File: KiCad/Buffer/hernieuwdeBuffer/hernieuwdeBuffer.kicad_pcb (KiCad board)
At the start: 2 copper layers, 90.2 x 77.5 mm, 38 parts, among them J1 Conn_01x04_Female, J2 12V DC, J3 Rood, J4 Groen, J5 Oranje1, J6 Oranje2, SW1 ENABLE, SW2 BOOT, T1 signaal oranje, T10 o3r, T11 o4r, T12 o5r, T13 06r, T14 r1, T15 r2, T16 r3, T17 r4, T18 r5, T19 g1, T2 o1g, T20 g2, T21 g3, T22 g4, T23 g5, T3 o2g, T4 o3g, T5 o4g, T6 o5g, T7 06g, T8 o1r, T9 o2r, U1 ESP32-WROOM-32E_(16MB)

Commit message: kicad
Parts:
- R1: footprint libraries:RESC6332X65N -> Resistor_SMD:R_0805_2012Metric
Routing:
- net Net-(C1-Pad2): track 20.9 -> 21.9 mm, vias 0 -> 1

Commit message: updates standaard schema
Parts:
- added C1: 1u, Capacitor_SMD:C_0805_2012Metric, F.Cu at (138.0, 145.7)
- added R1: 10k, libraries:RESC6332X65N, F.Cu at (120.3, 154.2)
- added R2: 10k, libraries:RESC6332X65N, F.Cu at (129.0, 154.2)
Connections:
- SW1 pad 1: Net-(C1-Pad2) -> Net-(U1-Pad25)
- SW1 pad 2: Net-(C1-Pad2) -> Net-(U1-Pad3)
- SW2 pad 1: Net-(SW2-Pad1) -> Net-(U1-Pad25)
- SW2 pad 2: Net-(SW2-Pad1) -> Net-(U1-Pad25)
- U1 pad 25: Net-(SW2-Pad1) -> Net-(U1-Pad25)
- U1 pad 3: Net-(R1-Pad2) -> Net-(U1-Pad3)
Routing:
- net r5: track 15.6 -> 0.00 mm, vias 1 -> 0
- net GND: track 209.5 -> 225.1 mm, vias 0 -> 1
- net Net-(U1-Pad25): track 0.00 -> 11.3 mm
- net Net-(SW2-Pad1): track 11.3 -> 0.00 mm
- net Net-(C1-Pad2): track 21.9 -> 13.4 mm
- net Net-(U1-Pad3): track 0.00 -> 3.77 mm
- net Net-(R1-Pad2): track 3.77 -> 0.00 mm

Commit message: kicad aanpassingen buffer
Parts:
- removed the C1 at (105.0, 75.8)
- removed the R1 at (118.9, 83.8)
- R1, R2: footprint libraries:RESC6332X65N -> Resistor_SMD:R_0805_2012Metric
- moved C1 73.2 mm to (115.0, 76.2), turned to 90 degrees
- moved R1 70.2 mm to (118.2, 84.1), turned to -90 degrees
- moved R2 48.9 mm to (130.6, 105.3), turned to 90 degrees
- moved SW1 4.77 mm to (107.8, 72.9)
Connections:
- SW1 pad 1: Net-(U1-Pad25) -> Net-(U1-Pad3)
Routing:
- net Net-(U1-Pad3): track 3.77 -> 39.0 mm, vias 0 -> 2
- net r5: track 0.00 -> 27.2 mm, vias 0 -> 1
- net GND: track 225.1 -> 251.3 mm, vias 1 -> 2
- net Net-(T1-Pad3): track 24.6 -> 44.6 mm
- net Net-(C1-Pad2): track 13.4 -> 0.00 mm, vias 1 -> 0
- net +3V3: track 64.8 -> 77.1 mm, vias 2 -> 1
- net Net-(U1-Pad25): track 11.3 -> 18.8 mm
- net g2: track 27.3 -> 34.0 mm
- net o1g: track 27.8 -> 33.3 mm
- net r2: track 15.1 -> 17.8 mm
- net o2g: track 24.6 -> 27.0 mm
- net o3g: track 21.9 -> 24.2 mm
- net r3: track 12.9 -> 15.0 mm
- net o6g: track 24.4 -> 26.5 mm
- net o4g: track 19.1 -> 21.1 mm
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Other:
- board text added: "BUFFER"

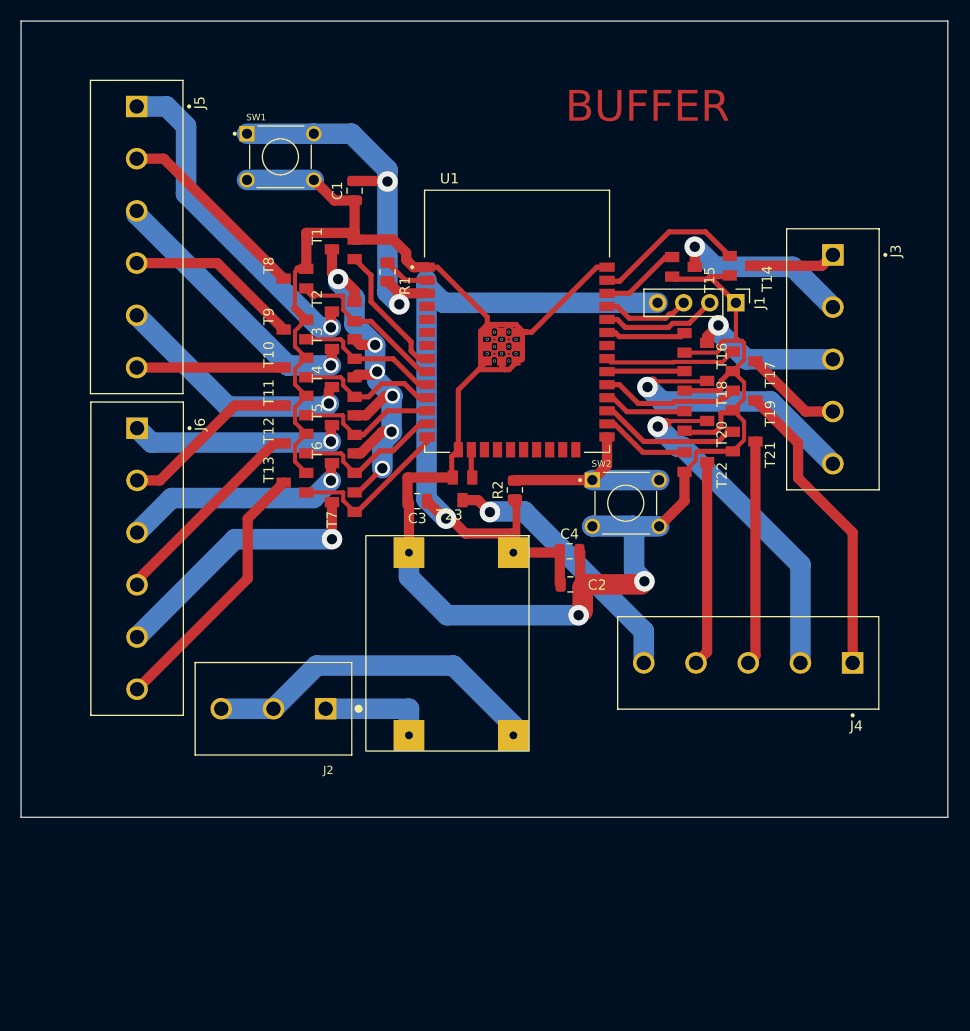
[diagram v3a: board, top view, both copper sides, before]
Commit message: update buffer
enkel schema van de buffer is volledig in orde met LDO!!!
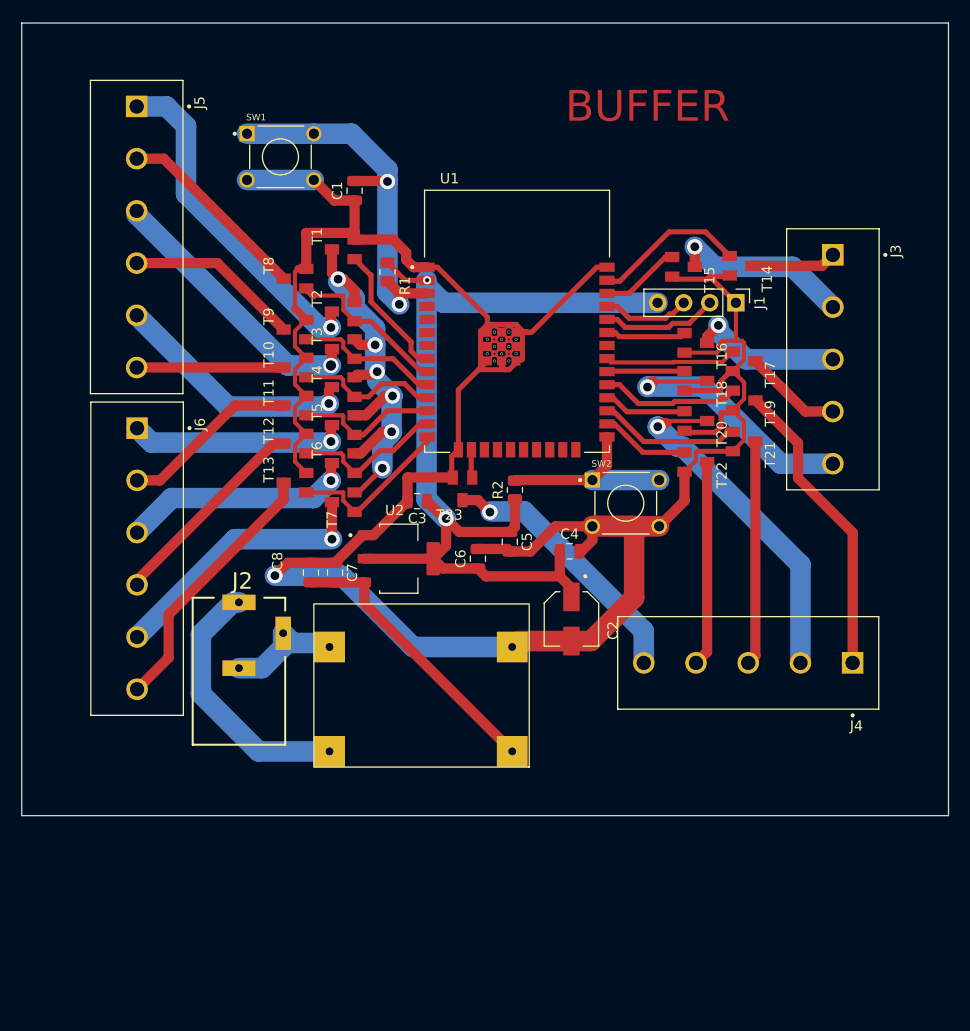
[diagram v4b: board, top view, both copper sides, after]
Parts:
- added C5: 0.1u, Capacitor_SMD:C_0805_2012Metric, F.Cu at (130.1, 110.3)
- added C6: 4.7u, Capacitor_SMD:C_0805_2012Metric, F.Cu at (127.0, 112.0)
- added C7: 0.1u, Capacitor_SMD:C_0805_2012Metric, F.Cu at (113.1, 113.3)
- added C8: 4.7u, Capacitor_SMD:C_0805_2012Metric, F.Cu at (110.8, 113.3)
- added U2: AMS1117, libraries:SOT229P700X180-4N, F.Cu at (119.3, 112.0)
- C2: footprint Capacitor_SMD:C_0805_2012Metric -> libraries:CAP_EEE0JA101WR
- J2: value 12V DC -> DCJ200-10-A-XX-X_REVA; footprint libraries:TE_282841-3 -> libraries:GCT_DCJ200-10-A-XX-X_REVA
- moved J2 4.96 mm to (103.8, 123.0), turned to 0 degrees
- moved PS1 4.88 mm to (121.5, 124.4), turned to 180 degrees
- moved C2 3.36 mm to (136.1, 117.9), turned to -90 degrees
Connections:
- PS1 pad 1a: Net-(J2-Pad2) -> Net-(J2-Pad1)
- PS1 pad 2a: Net-(J2-Pad1) -> Net-(J2-Pad2)
- PS1 pad 3a: +3V3 -> Net-(PS1-Pad3a)
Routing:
- net GND: track 251.3 -> 285.4 mm, vias 2 -> 1
- net Net-(PS1-Pad3a): track 0.00 -> 27.6 mm
- net Net-(J2-Pad2): track 33.5 -> 11.6 mm
- net +3V3: track 77.1 -> 94.4 mm, vias 1 -> 2
- net Net-(J2-Pad1): track 10.7 -> 25.6 mm
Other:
- board size 90.2 x 77.5 mm -> 90.2 x 77.1 mm

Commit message: aanpassingen 11/04 kicad
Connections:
- J2 pad 2: Net-(J2-Pad2) -> GND
- J2 pad 3: Net-(J2-Pad2) -> GND
- PS1 pad 2a: Net-(J2-Pad2) -> GND
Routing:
- net Net-(J2-Pad2): track 11.6 -> 0.00 mm
- net GND: track 285.4 -> 295.9 mm, vias 1 -> 0
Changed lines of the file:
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@@
   (net 64 "Net-(J2-Pad1)")
   (net 65 "Net-(R2-Pad2)")
-  (net 66 "Net-(J2-Pad2)")
   (footprint "libraries:SOT23" (layer "F.Cu")
     (at 148.2 91 -90)
@@
       (net 51 "unconnected-(PS1-Pad1b)") (pinfunction "+Vin") (pintype "power_in+no_connect"))
     (pad "2a" thru_hole rect (at 8.89 3.81 180) (size 3 3) (drill 0.762) (layers *.Cu *.Mask)
-      (net 66 "Net-(J2-Pad2)") (pinfunction "-Vin") (pintype "power_in"))
+      (net 1 "GND") (pinfunction "-Vin") (pintype "power_in"))
     (pad "2b" thru_hole circle (at 8.89 6.35 180) (size 0.05 0.05) (drill 0.762) (layers *.Cu *.Mask)
       (net 52 "unconnected-(PS1-Pad2b)") (pinfunction "-Vin") (pintype "power_in+no_connect"))
@@
       (net 64 "Net-(J2-Pad1)") (pintype "passive"))
     (pad "2" thru_hole rect (at 0 -0.3 180) (size 3.24 1.524) (drill 0.762) (layers *.Cu *.Mask)
-      (net 66 "Net-(J2-Pad2)") (pintype "passive"))
+      (net 1 "GND") (pintype "passive"))
     (pad "3" thru_hole rect (at 4.3 -3.7 90) (size 3.24 1.524) (drill 0.762) (layers *.Cu *.Mask)
-      (net 66 "Net-(J2-Pad2)") (pintype "passive"))
+      (net 1 "GND") (pintype "passive"))
   )
   (footprint "Resistor_SMD:R_0805_2012Metric" (layer "F.Cu")
@@
   (segment (start 131.79 89.96) (end 131.329521 89.96) (width 0.5) (layer "F.Cu") (net 1))
   (segment (start 150.649511 90.950489) (end 150.8 90.8) (width 0.4) (layer "F.Cu") (net 1))
-  (segment (start 108.5 112.4) (end 107.25 113.65) (width 1) (layer "F.Cu") (net 1))
   (segment (start 130.71 89.21) (end 131.46 89.96) (width 0.5) (layer "F.Cu") (net 1))
   (segment (start 150.1 99.7) (end 150.650489 99.149511) (width 0.5) (layer "F.Cu") (net 1))
@@
   (segment (start 150.650489 94.700489) (end 150.650489 95.449511) (width 0.5) (layer "F.Cu") (net 1))
   (segment (start 152.9 100.45) (end 151.8 101.55) (width 0.4) (layer "F.Cu") (net 1))
+  (segment (start 110.75 112.4) (end 110.358 112.4) (width 1) (layer "F.Cu") (net 1))
   (segment (start 130.036136 93.61) (end 130.71 92.936136) (width 0.5) (layer "F.Cu") (net 1))
   (segment (start 127.91 92.76) (end 128.404521 92.265479) (width 0.25) (layer "F.Cu") (net 1))
@@
   (segment (start 147.25 99.7) (end 150.1 99.7) (width 0.5) (layer "F.Cu") (net 1))
   (segment (start 128.404521 89.465479) (end 128.815479 89.465479) (width 0.25) (layer "F.Cu") (net 1))
+  (segment (start 108.331 116.361) (end 112.56 120.59) (width 1) (layer "F.Cu") (net 1))
   (segment (start 152.9 98.65) (end 152.9 100.45) (width 0.4) (layer "F.Cu") (net 1))
   (segment (start 109.200489 89.849511) (end 109.200489 91.350489) (width 0.4) (layer "F.Cu") (net 1))
@@
   (segment (start 113.035 77.15) (end 115 77.15) (width 1) (layer "F.Cu") (net 1))
   (segment (start 115.955 109.71) (end 116.84 109.71) (width 1) (layer "F.Cu") (net 1))
+  (segment (start 110.358 112.4) (end 108.331 114.427) (width 1) (layer "F.Cu") (net 1))
   (segment (start 129.31 91.36) (end 129.804521 91.854521) (width 0.25) (layer "F.Cu") (net 1))
   (segment (start 131.46 89.96) (end 131.79 89.96) (width 0.5) (layer "F.Cu") (net 1))
@@
   (segment (start 129.804521 90.454521) (end 129.804521 90.865479) (width 0.25) (layer "F.Cu") (net 1))
   (segment (start 110.3 88.75) (end 109.2 87.65) (width 0.75) (layer "F.Cu") (net 1))
-  (segment (start 110.75 112.4) (end 108.5 112.4) (width 1) (layer "F.Cu") (net 1))
   (segment (start 109.2 87.65) (end 109.2 84.1) (width 0.4) (layer "F.Cu") (net 1))
+  (segment (start 108.331 114.427) (end 108.331 116.361) (width 1) (layer "F.Cu") (net 1))
   (segment (start 127.26 91.29) (end 127.26 89.86) (width 0.5) (layer "F.Cu") (net 1))
   (segment (start 111.035 75.15) (end 113.035 77.15) (width 1) (layer "F.Cu") (net 1))
@@
   (segment (start 129.31 93.28) (end 129.31 92.76) (width 0.5) (layer "F.Cu") (net 1))
   (segment (start 151.8 97.8) (end 151.8 97.55) (width 0.4) (layer "F.Cu") (net 1))
-  (via (at 107.25 113.65) (size 1.5) (drill 0.85) (layers "F.Cu" "B.Cu") (free) (net 1))
+  (segment (start 106 122.65) (end 108.05 120.6) (width 2) (layer "B.Cu") (net 1))
+  (segment (start 108.05 119.25) (end 109 120.2) (width 2) (layer "B.Cu") (net 1))
   (segment (start 104.535 75.15) (end 111.035 75.15) (width 2) (layer "B.Cu") (net 1))
-  (segment (start 113.75 113.65) (end 107.25 113.65) (width 2) (layer "B.Cu") (net 1))
-  (segment (start 130.34 120.59) (end 120.69 120.59) (width 2) (layer "B.Cu") (net 1))
-  (segment (start 120.69 120.59) (end 113.75 113.65) (width 2) (layer "B.Cu") (net 1))
+  (segment (start 112.56 120.59) (end 130.34 120.59) (width 1) (layer "B.Cu") (net 1))
+  (segment (start 109 120.2) (end 112.17 120.2) (width 2) (layer "B.Cu") (net 1))
+  (segment (start 103.75 122.65) (end 106 122.65) (width 2) (layer "B.Cu") (net 1))
+  (segment (start 108.05 120.6) (end 108.05 119.25) (width 2) (layer "B.Cu") (net 1))
+  (segment (start 112.17 120.2) (end 112.56 120.59) (width 2) (layer "B.Cu") (net 1))
   (segment (start 160.4775 83.5) (end 161.5375 82.44) (width 1) (layer "F.Cu") (net 2))
   (segment (start 153.7 83.5) (end 160.4775 83.5) (width 1) (layer "F.Cu") (net 2))
@@
   (segment (start 139.56 100.15) (end 139.56 102.925) (width 1) (layer "F.Cu") (net 65))
   (segment (start 144.635 104.35) (end 138.135 104.35) (width 2) (layer "B.Cu") (net 65))
-  (segment (start 106 122.65) (end 108.05 120.6) (width 2) (layer "B.Cu") (net 66))
-  (segment (start 108.05 119.25) (end 109 120.2) (width 2) (layer "B.Cu") (net 66))
-  (segment (start 109 120.2) (end 112.17 120.2) (width 2) (layer "B.Cu") (net 66))
-  (segment (start 103.75 122.65) (end 106 122.65) (width 2) (layer "B.Cu") (net 66))
-  (segment (start 108.05 120.6) (end 108.05 119.25) (width 2) (layer "B.Cu") (net 66))
-  (segment (start 112.17 120.2) (end 112.56 120.59) (width 2) (layer "B.Cu") (net 66))
 )
